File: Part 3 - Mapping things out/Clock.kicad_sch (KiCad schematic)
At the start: 47 parts, among them SW3 STEP, SW4 MODE, SW5 SPEED, SW6 BOOT MODE, SW7 BOOT SPEED, U1 74HC14, U3 74HC74, U4 LMC555, U5 74HC74, U7 74HC151, X1 14.7456MHz

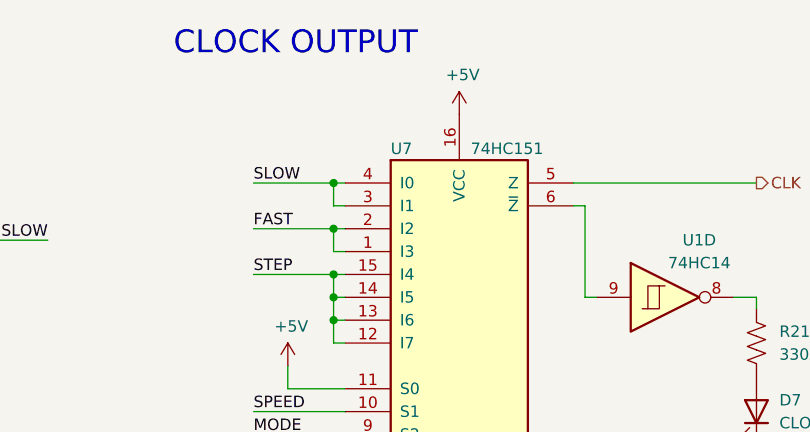
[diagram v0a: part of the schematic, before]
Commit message: Updated glue logic and bank switching
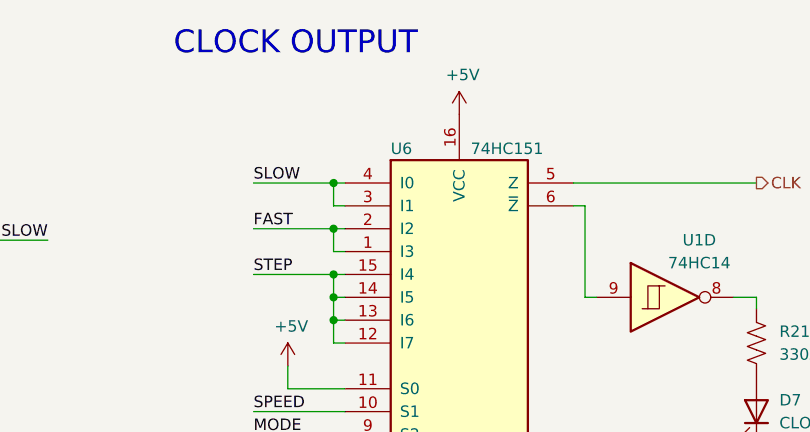
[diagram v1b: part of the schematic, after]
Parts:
- renumbered U7 to U6
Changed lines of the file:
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@@
   (symbol (lib_id "power:+5V") (at 149.86 38.1 0) (unit 1)
     (in_bom yes) (on_board yes)
-    (property "Reference" "#PWR041" (id 0) (at 149.86 41.91 0)
+    (property "Reference" "#PWR033" (id 0) (at 149.86 41.91 0)
       (effects (font (size 1.27 1.27)) hide)
     )
@@
   (symbol (lib_id "power:+5V") (at 224.79 106.68 0) (unit 1)
     (in_bom yes) (on_board yes)
-    (property "Reference" "#PWR036" (id 0) (at 224.79 110.49 0)
+    (property "Reference" "#PWR045" (id 0) (at 224.79 110.49 0)
       (effects (font (size 1.27 1.27)) hide)
     )
@@
   (symbol (lib_id "power:GND") (at 224.79 132.08 0) (unit 1)
     (in_bom yes) (on_board yes)
-    (property "Reference" "#PWR037" (id 0) (at 224.79 138.43 0)
+    (property "Reference" "#PWR046" (id 0) (at 224.79 138.43 0)
       (effects (font (size 1.27 1.27)) hide)
     )
@@
   (symbol (lib_id "power:+5V") (at 125.73 33.02 0) (unit 1)
     (in_bom yes) (on_board yes)
-    (property "Reference" "#PWR034" (id 0) (at 125.73 36.83 0)
+    (property "Reference" "#PWR029" (id 0) (at 125.73 36.83 0)
       (effects (font (size 1.27 1.27)) hide)
     )
@@
   (symbol (lib_id "power:GND") (at 125.73 62.23 0) (unit 1)
     (in_bom yes) (on_board yes)
-    (property "Reference" "#PWR035" (id 0) (at 125.73 68.58 0)
+    (property "Reference" "#PWR030" (id 0) (at 125.73 68.58 0)
       (effects (font (size 1.27 1.27)) hide)
     )
@@
   (symbol (lib_id "power:+5V") (at 149.86 53.34 180) (unit 1)
     (in_bom yes) (on_board yes)
-    (property "Reference" "#PWR042" (id 0) (at 149.86 49.53 0)
+    (property "Reference" "#PWR034" (id 0) (at 149.86 49.53 0)
       (effects (font (size 1.27 1.27)) hide)
     )
@@
   (symbol (lib_id "power:+5V") (at 163.83 93.98 0) (unit 1)
     (in_bom yes) (on_board yes)
-    (property "Reference" "#PWR047" (id 0) (at 163.83 97.79 0)
+    (property "Reference" "#PWR035" (id 0) (at 163.83 97.79 0)
       (effects (font (size 1.27 1.27)) hide)
     )
@@
   (symbol (lib_id "power:GND") (at 237.49 132.08 0) (unit 1)
     (in_bom yes) (on_board yes)
-    (property "Reference" "#PWR040" (id 0) (at 237.49 138.43 0)
+    (property "Reference" "#PWR048" (id 0) (at 237.49 138.43 0)
       (effects (font (size 1.27 1.27)) hide)
     )
@@
   (symbol (lib_id "power:GND") (at 212.09 132.08 0) (unit 1)
     (in_bom yes) (on_board yes)
-    (property "Reference" "#PWR031" (id 0) (at 212.09 138.43 0)
+    (property "Reference" "#PWR042" (id 0) (at 212.09 138.43 0)
       (effects (font (size 1.27 1.27)) hide)
     )
@@
   (symbol (lib_id "power:GND") (at 246.38 67.31 0) (unit 1)
     (in_bom yes) (on_board yes)
-    (property "Reference" "#PWR053" (id 0) (at 246.38 73.66 0)
+    (property "Reference" "#PWR049" (id 0) (at 246.38 73.66 0)
       (effects (font (size 1.27 1.27)) hide)
     )
@@
   (symbol (lib_id "power:+5V") (at 194.31 57.15 0) (unit 1)
     (in_bom yes) (on_board yes)
-    (property "Reference" "#PWR049" (id 0) (at 194.31 60.96 0)
+    (property "Reference" "#PWR039" (id 0) (at 194.31 60.96 0)
       (effects (font (size 1.27 1.27)) hide)
     )
@@
   (symbol (lib_id "power:GND") (at 180.34 162.56 0) (unit 1)
     (in_bom yes) (on_board yes)
-    (property "Reference" "#PWR046" (id 0) (at 180.34 168.91 0)
+    (property "Reference" "#PWR038" (id 0) (at 180.34 168.91 0)
       (effects (font (size 1.27 1.27)) hide)
     )
@@
   (symbol (lib_id "power:GND") (at 195.58 80.01 0) (unit 1)
     (in_bom yes) (on_board yes)
-    (property "Reference" "#PWR050" (id 0) (at 195.58 86.36 0)
+    (property "Reference" "#PWR040" (id 0) (at 195.58 86.36 0)
       (effects (font (size 1.27 1.27)) hide)
     )
@@
   (symbol (lib_id "power:+5V") (at 163.83 109.22 180) (unit 1)
     (in_bom yes) (on_board yes)
-    (property "Reference" "#PWR048" (id 0) (at 163.83 105.41 0)
+    (property "Reference" "#PWR036" (id 0) (at 163.83 105.41 0)
       (effects (font (size 1.27 1.27)) hide)
     )
@@
   (symbol (lib_id "74xx:74LS151") (at 213.36 52.07 0) (unit 1)
     (in_bom yes) (on_board yes)
-    (property "Reference" "U7" (id 0) (at 205.74 33.02 0)
+    (property "Reference" "U6" (id 0) (at 205.74 33.02 0)
       (effects (font (size 1.27 1.27)) (justify left))
     )
@@
   (symbol (lib_id "power:+5V") (at 212.09 106.68 0) (unit 1)
     (in_bom yes) (on_board yes)
-    (property "Reference" "#PWR030" (id 0) (at 212.09 110.49 0)
+    (property "Reference" "#PWR041" (id 0) (at 212.09 110.49 0)
       (effects (font (size 1.27 1.27)) hide)
     )
@@
   (symbol (lib_id "power:+5V") (at 237.49 106.68 0) (unit 1)
     (in_bom yes) (on_board yes)
-    (property "Reference" "#PWR039" (id 0) (at 237.49 110.49 0)
+    (property "Reference" "#PWR047" (id 0) (at 237.49 110.49 0)
       (effects (font (size 1.27 1.27)) hide)
     )
@@
   (symbol (lib_id "power:+5V") (at 180.34 149.86 0) (unit 1)
     (in_bom yes) (on_board yes)
-    (property "Reference" "#PWR045" (id 0) (at 180.34 153.67 0)
+    (property "Reference" "#PWR037" (id 0) (at 180.34 153.67 0)
       (effects (font (size 1.27 1.27)) hide)
     )
@@
   (symbol (lib_id "power:+5V") (at 135.89 91.44 0) (unit 1)
     (in_bom yes) (on_board yes) (fields_autoplaced)
-    (property "Reference" "#PWR032" (id 0) (at 135.89 95.25 0)
+    (property "Reference" "#PWR031" (id 0) (at 135.89 95.25 0)
       (effects (font (size 1.27 1.27)) hide)
     )
@@
   (symbol (lib_id "power:GND") (at 213.36 77.47 0) (unit 1)
     (in_bom yes) (on_board yes) (fields_autoplaced)
-    (property "Reference" "#PWR052" (id 0) (at 213.36 83.82 0)
+    (property "Reference" "#PWR044" (id 0) (at 213.36 83.82 0)
       (effects (font (size 1.27 1.27)) hide)
     )
@@
   (symbol (lib_id "power:GND") (at 135.89 110.49 0) (unit 1)
     (in_bom yes) (on_board yes) (fields_autoplaced)
-    (property "Reference" "#PWR033" (id 0) (at 135.89 116.84 0)
+    (property "Reference" "#PWR032" (id 0) (at 135.89 116.84 0)
       (effects (font (size 1.27 1.27)) hide)
     )
@@
   (symbol (lib_id "power:+5V") (at 213.36 29.21 0) (unit 1)
     (in_bom yes) (on_board yes)
-    (property "Reference" "#PWR051" (id 0) (at 213.36 33.02 0)
-      (effects (font (size 1.27 1.27)) hide)
-    )
+    (property "Reference" "#PWR043" (id 0) (at 213.36 33.02 0)
+      (effects (font (size 1.27 1.27)) hide)
+    )

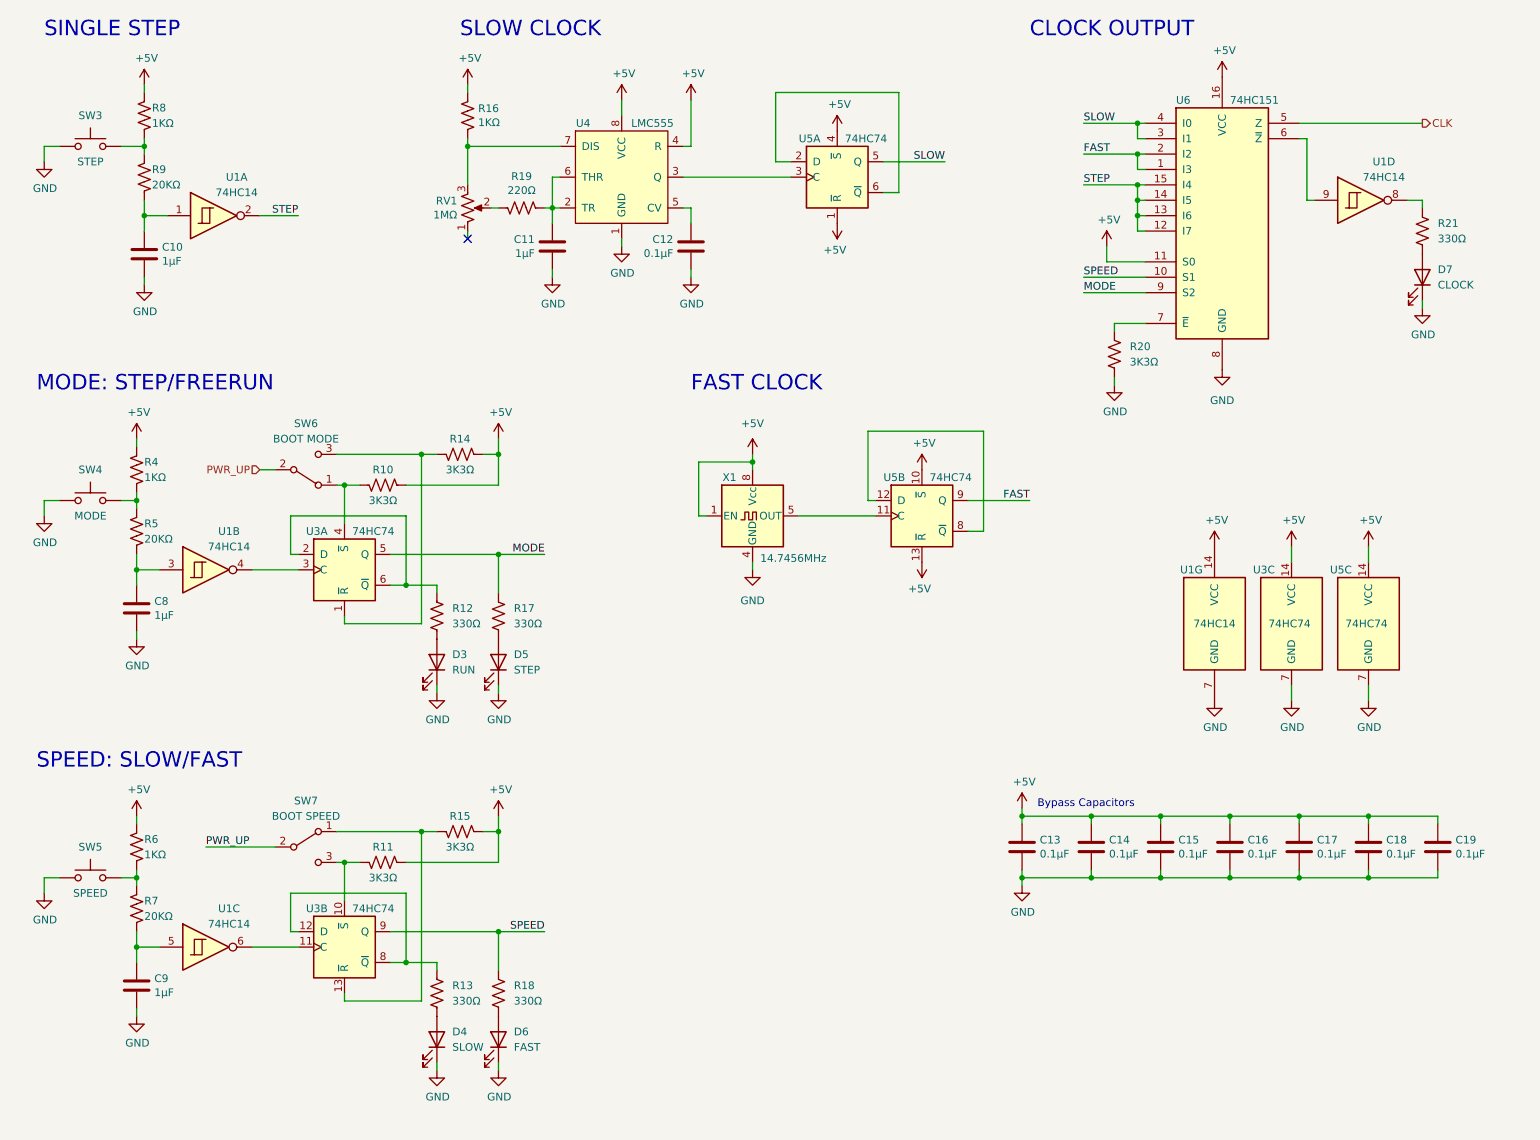
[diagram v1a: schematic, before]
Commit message: Backplane PCB sent out, and experimented with clock options
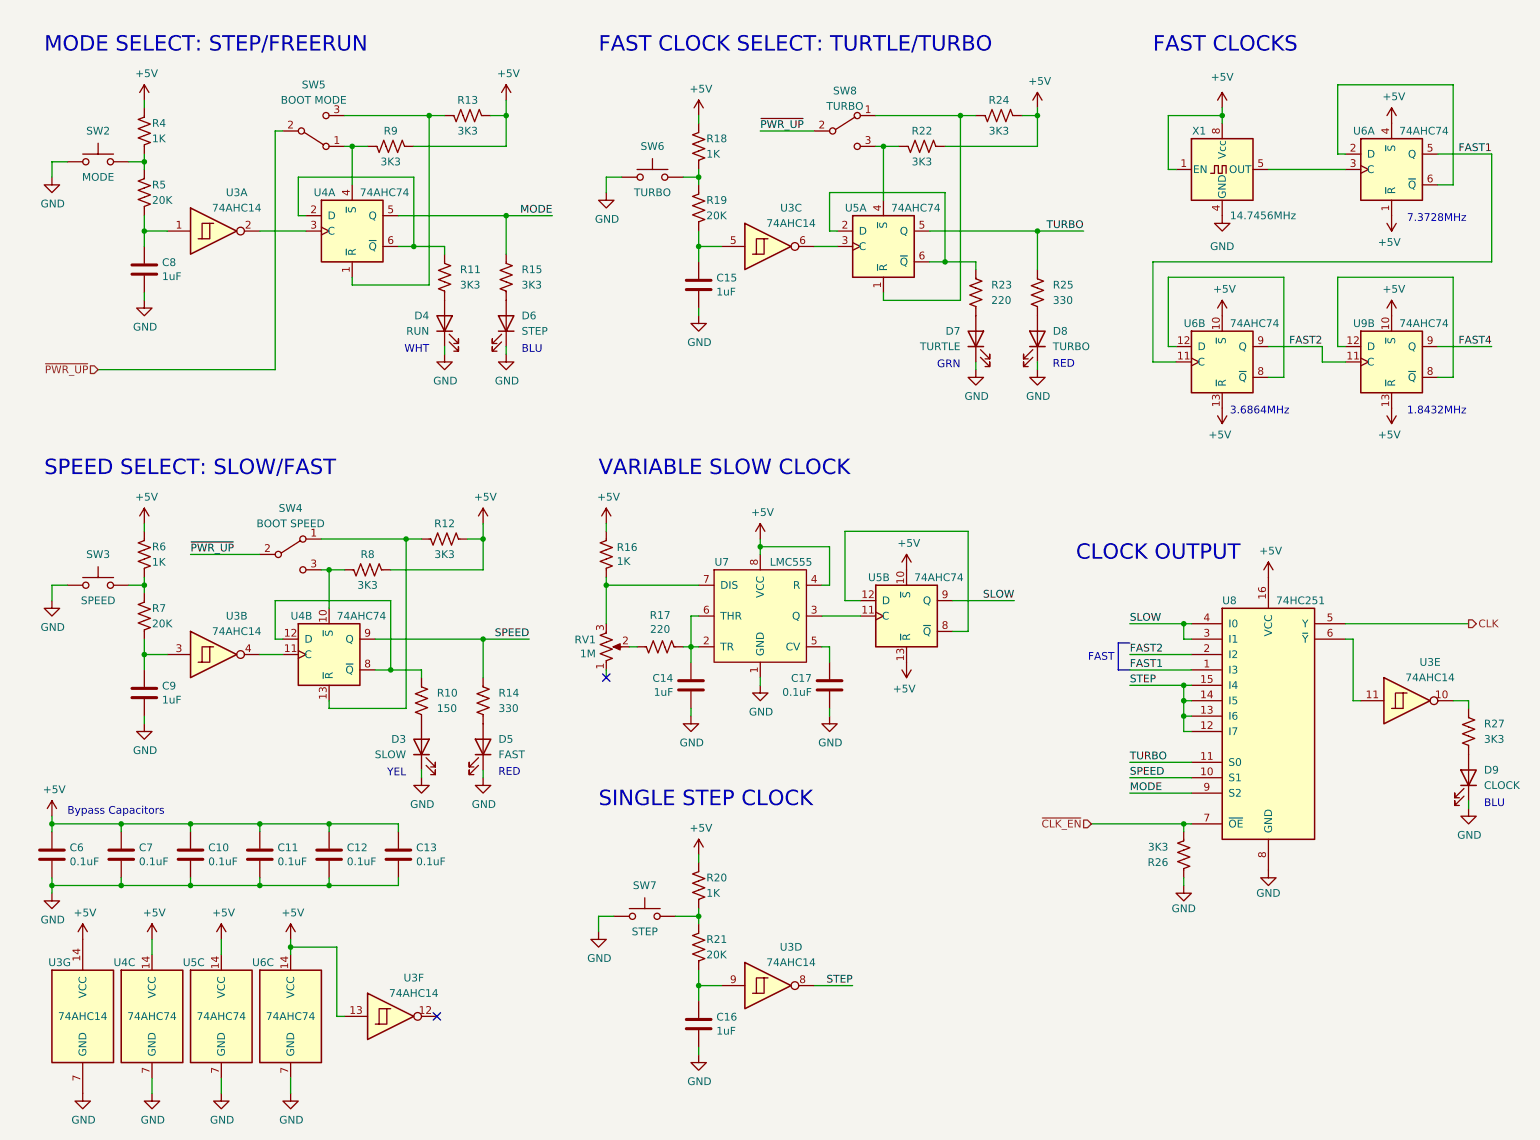
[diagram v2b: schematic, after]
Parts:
- removed C19: 0.1µF, Capacitor_THT:C_Disc_D3.0mm_W1.6mm_P2.50mm, symbol Device:C
- removed unit 7 of U1
- removed U6: 74HC151, symbol 74xx:74LS151
- added C15: 1uF, Capacitor_THT:C_Disc_D3.0mm_W1.6mm_P2.50mm, symbol Device:C
- added D7: TURTLE, LED_THT:LED_D3.0mm, symbol Device:LED
- added D8: TURBO, LED_THT:LED_D3.0mm, symbol Device:LED
- added R18: 1K, Resistor_THT:R_Axial_DIN0207_L6.3mm_D2.5mm_P10.16mm_Horizontal, symbol Device:R_US
- added R19: 20K, Resistor_THT:R_Axial_DIN0207_L6.3mm_D2.5mm_P10.16mm_Horizontal, symbol Device:R_US
- added R22, R24: 3K3, Resistor_THT:R_Axial_DIN0207_L6.3mm_D2.5mm_P10.16mm_Horizontal, symbol Device:R_US
- added R23: 220, Resistor_THT:R_Axial_DIN0207_L6.3mm_D2.5mm_P10.16mm_Horizontal, symbol Device:R_US
- added R25: 330, Resistor_THT:R_Axial_DIN0207_L6.3mm_D2.5mm_P10.16mm_Horizontal, symbol Device:R_US
- added SW6: TURBO, Button_Switch_THT:SW_PUSH_6mm, symbol Switch:SW_Push
- added SW8: TURBO, 0_Z80_Library:Microswitch_2.54mm_spacing, symbol Switch:SW_SPDT
- added unit 6 of U3
- added unit 7 of U3
- added unit 3 of U3
- added unit 1 of U5
- added unit 3 of U6
- added unit 2 of U6
- added U8: 74HC251, Package_DIP:DIP-14_W7.62mm_Socket, symbol 74xx:74LS251
- added U9: 74AHC74, Package_DIP:DIP-14_W7.62mm_Socket, symbol 74xx:74HC74
- C10: renamed from C15; value 0.1µF -> 0.1uF
- C11: renamed from C16; value 0.1µF -> 0.1uF
- C12: renamed from C17; value 0.1µF -> 0.1uF
- C13: renamed from C18; value 0.1µF -> 0.1uF
- C14: renamed from C11; value 1µF -> 1uF
- C16: renamed from C10; value 1µF -> 1uF
- C17: renamed from C12; value 0.1µF -> 0.1uF
- C6: renamed from C13; value 0.1µF -> 0.1uF
- C7: renamed from C14; value 0.1µF -> 0.1uF
- C8, C9: value 1µF -> 1uF
- R10: renamed from R13; value 330Ω -> 150
- R11: renamed from R12; value 330Ω -> 3K3
- R12: renamed from R15; value 3K3Ω -> 3K3; footprint Resistor_THT:R_Axial_DIN0207_L6.3mm_D2.5mm_P7.62mm_Horizontal -> Resistor_THT:R_Axial_DIN0207_L6.3mm_D2.5mm_P10.16mm_Horizontal
- R13: renamed from R14; value 3K3Ω -> 3K3; footprint Resistor_THT:R_Axial_DIN0207_L6.3mm_D2.5mm_P7.62mm_Horizontal -> Resistor_THT:R_Axial_DIN0207_L6.3mm_D2.5mm_P10.16mm_Horizontal
- R14: renamed from R18; value 330Ω -> 330
- R15: renamed from R17; value 330Ω -> 3K3
- R16, R4, R6: value 1KΩ -> 1K; footprint Resistor_THT:R_Axial_DIN0207_L6.3mm_D2.5mm_P7.62mm_Horizontal -> Resistor_THT:R_Axial_DIN0207_L6.3mm_D2.5mm_P10.16mm_Horizontal
- R17: renamed from R19; value 220Ω -> 220; footprint Resistor_THT:R_Axial_DIN0207_L6.3mm_D2.5mm_P7.62mm_Horizontal -> Resistor_THT:R_Axial_DIN0207_L6.3mm_D2.5mm_P10.16mm_Horizontal
- R20: renamed from R8; value 1KΩ -> 1K; footprint Resistor_THT:R_Axial_DIN0207_L6.3mm_D2.5mm_P7.62mm_Horizontal -> Resistor_THT:R_Axial_DIN0207_L6.3mm_D2.5mm_P10.16mm_Horizontal
- R21: renamed from R9; value 20KΩ -> 20K; footprint Resistor_THT:R_Axial_DIN0207_L6.3mm_D2.5mm_P7.62mm_Horizontal -> Resistor_THT:R_Axial_DIN0207_L6.3mm_D2.5mm_P10.16mm_Horizontal
- R26: renamed from R20; value 3K3Ω -> 3K3
- R27: renamed from R21; value 330Ω -> 3K3
- R5, R7: value 20KΩ -> 20K; footprint Resistor_THT:R_Axial_DIN0207_L6.3mm_D2.5mm_P7.62mm_Horizontal -> Resistor_THT:R_Axial_DIN0207_L6.3mm_D2.5mm_P10.16mm_Horizontal
- R8: renamed from R11; value 3K3Ω -> 3K3; footprint Resistor_THT:R_Axial_DIN0207_L6.3mm_D2.5mm_P7.62mm_Horizontal -> Resistor_THT:R_Axial_DIN0207_L6.3mm_D2.5mm_P10.16mm_Horizontal
- R9: renamed from R10; value 3K3Ω -> 3K3; footprint Resistor_THT:R_Axial_DIN0207_L6.3mm_D2.5mm_P7.62mm_Horizontal -> Resistor_THT:R_Axial_DIN0207_L6.3mm_D2.5mm_P10.16mm_Horizontal
- RV1: value 1MΩ -> 1M; footprint Potentiometer_THT:Potentiometer_Bourns_3386P_Vertical -> Potentiometer_THT:Potentiometer_Bourns_3299Y_Vertical
- SW4: renamed from SW7; footprint (none) -> 0_Z80_Library:Microswitch_2.54mm_spacing
- SW5: renamed from SW6; footprint (none) -> 0_Z80_Library:Microswitch_2.54mm_spacing
- U3: renamed from U1; value 74HC14 -> 74AHC14
- U4: renamed from U3; value 74HC74 -> 74AHC74
- U5: value 74HC74 -> 74AHC74
- U6: renamed from U5; value 74HC74 -> 74AHC74
- U7: renamed from U4; footprint Package_DIP:DIP-8_W7.62mm_Socket -> Package_DIP:DIP-14_W7.62mm_Socket
- renumbered D4 to D3, D3 to D4, D6 to D5, D5 to D6, D7 to D9, SW4 to SW2, SW5 to SW3, SW3 to SW7
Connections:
- net +5V: now also U5.10 (~{S}), U5.13 (~{R}), U6.1 (~{R}), U6.4 (~{S}), R18.1, R22.2, R24.2, U3.13, U3.14 (VCC), U6.10 (~{S}), U6.13 (~{R}), U6.14 (VCC), U8.16 (VCC), U9.10 (~{S}), U9.13 (~{R}); no longer U5.1 (~{R}), U5.4 (~{S}), U6.10 (~{S}), U6.13 (~{R})
- net CLK: now also U8.5 (Y)
- net GND: now also C15.2, D7.1 (K), D8.1 (K), SW6.2, U3.7 (GND), U6.7 (GND), U8.8 (GND)
- net MODE: now also U8.9 (S2)
- net SLOW: now also U5.9 (Q), U8.3 (I1), U8.4 (I0); no longer U5.5 (Q)
- net SPEED: now also U8.10 (S1)
- net STEP: now also U3.8, U8.12 (I7), U8.13 (I6), U8.14 (I5), U8.15 (I4); no longer U3.2
- net at U7.3 (Q): now also U5.11 (C); no longer U5.3 (C)
- net at C9.1, R7.1: now also U3.3; no longer U3.5
- net at X1.5 (OUT): now also U6.3 (C); no longer U6.11 (C)
- net ~{CLK_EN}: now reaches R26.1
- net ~{CLK_EN}: now also U8.7 (~{OE})
- net at C8.1, R5.1: now also U3.1; no longer U3.3
- net at C16.1, R21.1: now also U3.9; no longer U3.1
- net at R27.1: now also U3.10; no longer U3.8
- net at U4.11 (C): now also U3.4; no longer U3.6
- net at U4.3 (C): now also U3.2; no longer U3.4
- removed net FAST: U6.9 (Q)
- net PWR_UP renamed ~{PWR_UP}
- net ~{PWR_UP}: now also SW8.2 (B)
- new net: U5.12 (D), U5.8 (~{Q})
- new net: C15.1, R19.1, U3.5
- new net: R18.2, R19.2, SW6.1
- new net: D8.2 (A), R25.2
- new net: R22.1, SW8.3 (C), U5.4 (~{S})
- new net: R24.1, SW8.1 (A), U5.1 (~{R})
- new net: U3.11, U8.6 (~{Y})
- new net: U9.12 (D), U9.8 (~{Q})
- new net: U6.2 (D), U6.6 (~{Q})
- new net: R23.1, U5.2 (D), U5.6 (~{Q})
- new net: U3.6, U5.3 (C)
- new net: D7.2 (A), R23.2
- new net: U6.12 (D), U6.8 (~{Q})
- new net FAST1: U6.11 (C), U6.5 (Q), U8.1 (I3)
- new net FAST2: U6.9 (Q), U8.2 (I2), U9.11 (C)
- new net FAST4: U9.9 (Q)
- new net TURBO: R25.1, U5.5 (Q), U8.11 (S0)
- no-connect marks 1 -> 2
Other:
- note added: "1.8432MHz"
- note added: "3.6864MHz"
- note added: "7.3728MHz"
- note added: "BLU"
- note added: "FAST"
- note added: "FAST CLOCK SELECT: TURTLE/TURBO"
- note added: "FAST CLOCKS"
- note added: "GRN"
- note added: "MODE SELECT: STEP/FREERUN"
- note added: "RED"
- note added: "SINGLE STEP CLOCK"
- note added: "SPEED SELECT: SLOW/FAST"
- note added: "VARIABLE SLOW CLOCK"
- note added: "WHT"
- note added: "YEL"
- note removed: "FAST CLOCK"
- note removed: "MODE: STEP/FREERUN"
- note removed: "SINGLE STEP"
- note removed: "SLOW CLOCK"
- note removed: "SPEED: SLOW/FAST"
- company: Frederic Segard - aka: The Micro Hobbyist -> Frédéric Segard
- moved on the sheet: C10, C11, C12, C13, C14, C16, C17, C6, C7, C8, C9, D3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
